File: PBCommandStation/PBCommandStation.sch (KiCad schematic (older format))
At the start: 7 parts, among them P1 POCKETBEAGLE-P1, P2 POCKETBEAGLE-P2, Q101 PN2222A, U101 SN75ALS174

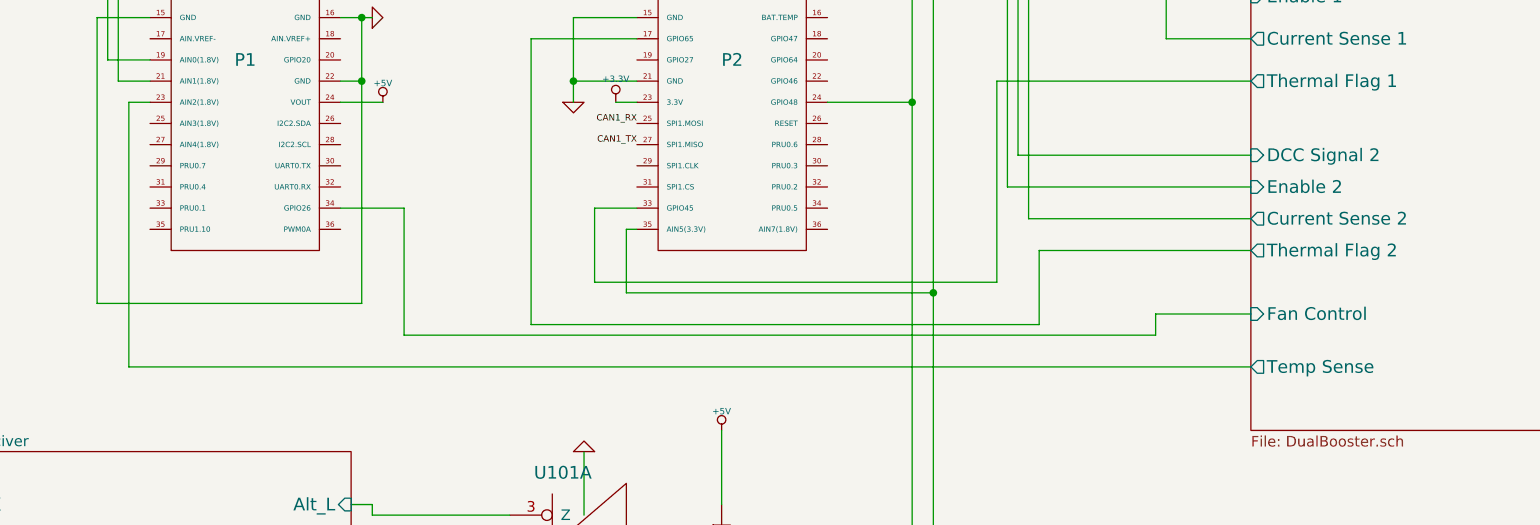
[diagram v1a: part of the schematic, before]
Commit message: Add Prog Ack Detect circuit.
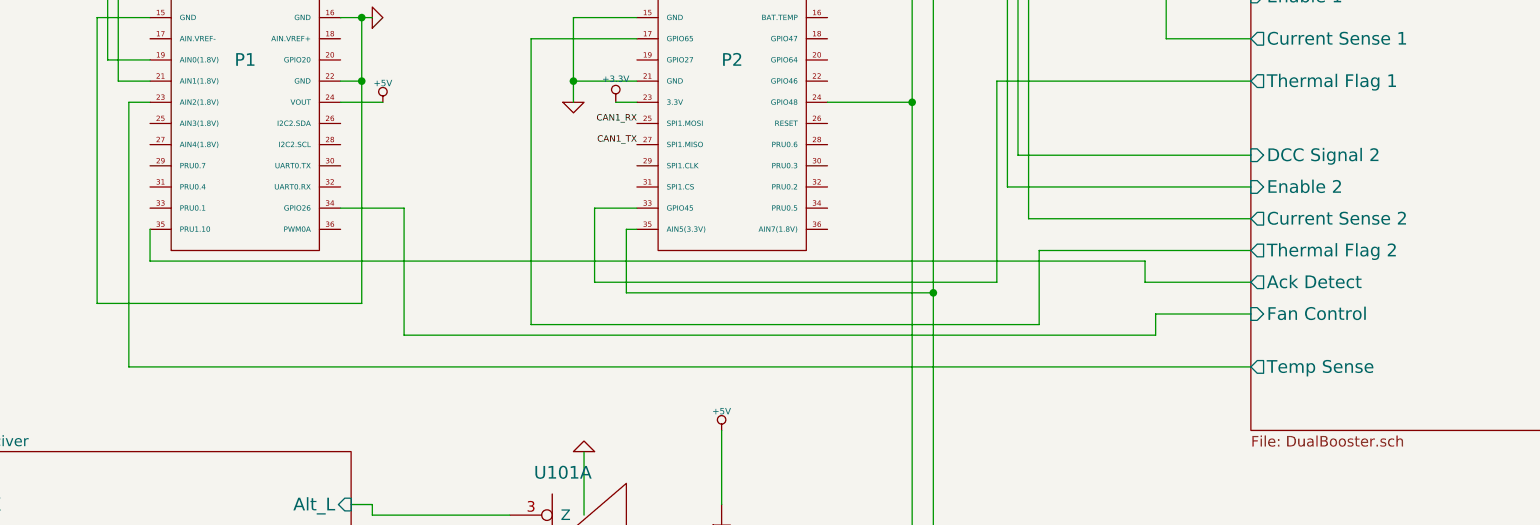
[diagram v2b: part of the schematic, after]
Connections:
- net Dual Booster/Ack Detect: now reaches P1.35 (PRU1.10)
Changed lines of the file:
@@
 Sheet 1 4
 Title ""
-Date "3 nov 2019"
+Date "10 nov 2019"
 Rev ""
 Comp ""
@@
 F10 "Fan Control" I L 7600 3750 60
 F11 "Temp Sense" O L 7600 4000 60
+F12 "Ack Detect" O L 7600 3600 60
 $EndSheet
 $Comp
@@
 Wire Wire Line
 	2300 2750 2400 2750
+Wire Wire Line
+	2400 3350 2400 3500
+Wire Wire Line
+	2400 3500 7100 3500
+Wire Wire Line
+	7100 3500 7100 3600
+Wire Wire Line
+	7100 3600 7600 3600
 $EndSCHEMATC
